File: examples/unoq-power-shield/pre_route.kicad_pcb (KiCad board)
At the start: 4 copper layers, 53.3 x 68.6 mm, 56 parts, among them J1 VIN 7-24V, J10 UNO PWR, J11 UNO ANALOG, J12 UNO D0-D7, J13 UNO D8-SCL, J2 5V OUT, J3 Qwiic, J4 Qwiic, J5 5V IO, Q1 BSS138LT1G, Q2 BSS138LT1G, Q3 BSS138LT1G, Q4 BSS138LT1G, Q5 AO4407A, U1 TPS54331DDAR, U2 INA226AIDGSR

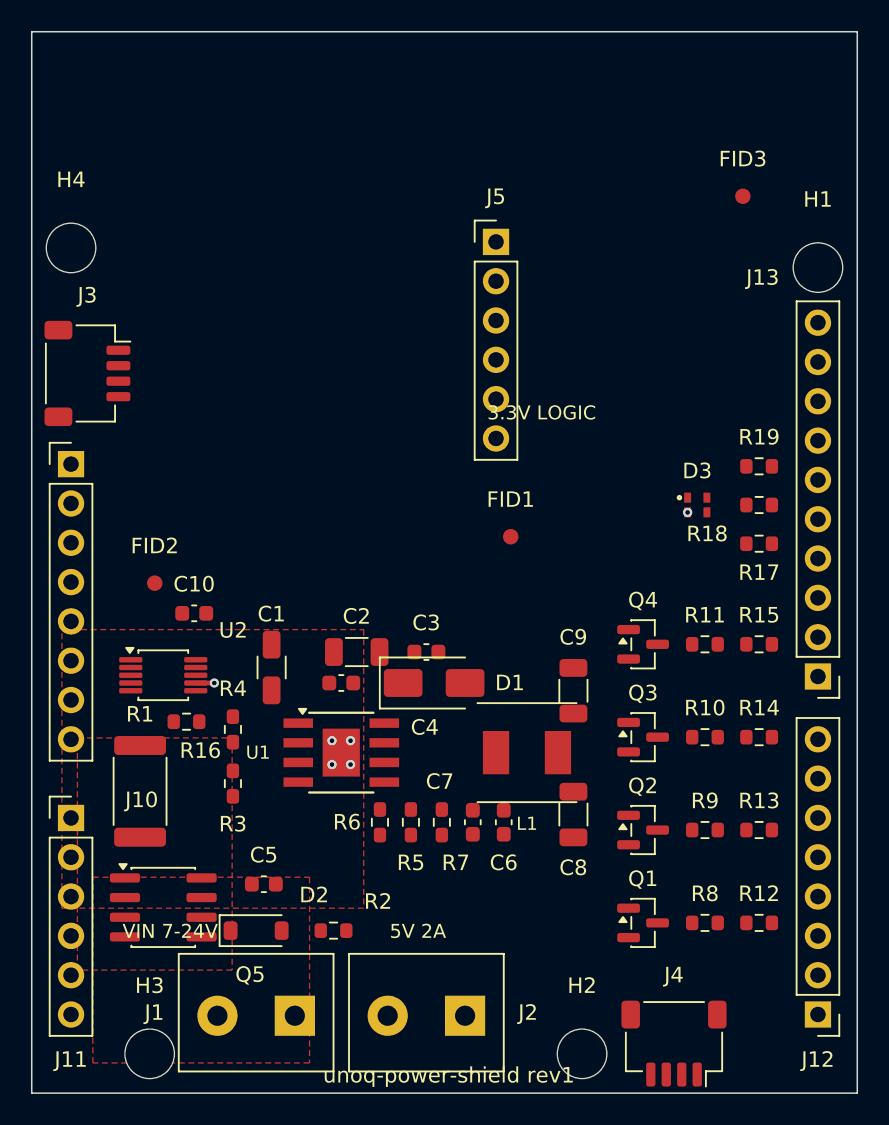
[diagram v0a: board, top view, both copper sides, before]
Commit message: Carry the silk fix into the pre-route snapshot too
route.py restarts from pre_route.kicad_pcb (`shutil.copyfile(snapshot,
board)` at step 0), so the snapshot still holding "3.3V LOGIC" on J5's
pads meant the next `make route` would have silently reinstated the
defect over the corrected board — with every gate still green, because
the gates would then be measuring the reverted silk.

Re-ran silk_finish against the snapshot with the corrected board.toml,
which is the same pass and order the build uses to produce it (zones ->
fanout -> fiducials -> keepouts -> silk -> fill -> snapshot). Warnings
empty; no copper touched.

Co-Authored-By: Claude Opus 5 (1M context) <noreply@anthropic.com>
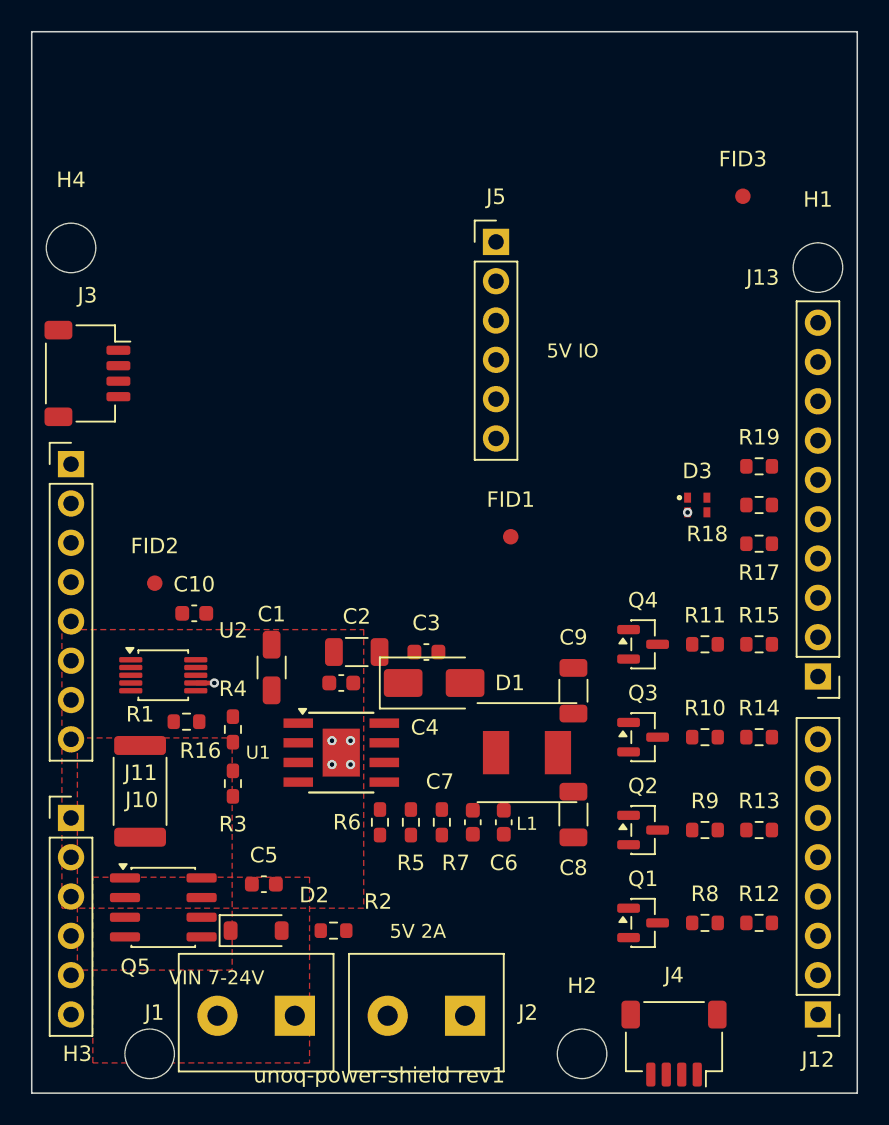
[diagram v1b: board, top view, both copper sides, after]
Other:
- board text added: "5V IO"
- board text removed: "3.3V LOGIC"

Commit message: Example: rotate J4 to face its edge, rebuild; all gates pass
J4 (Qwiic, SM04B-SRSS-TB) was at rotation 180 with its socket opening
into the board. Floorplan now rotation 0, y 3.2 -> 3.4 so the MP tabs
clear the 0.5 mm edge rule by 0.625 mm; the J4 copper_edge_clearance
ledger entry (a symptom of the rotation) is removed.

Rebuilt from netlist.csv in the pinned container (KiCad 10.0.5,
Freerouting 1.9.0) with the fixed pipeline. make check passes:
ERC 0 errors; pad angles all correct; DRC x5 13 errors, all ledgered,
identical every run, 0 unconnected, no stale entries; check_placement
11/0; validate_gerbers 15/0 with IPC-D-356 = netlist.csv 159/159.
drc_report.json, erc_report.json and img/*.png regenerated from the
rebuilt board. Still unfabricated; stock check and committing the exact
ordered package remain for order time (rev-1-plan.md).

Co-Authored-By: Claude Opus 5.5 <noreply@anthropic.com>
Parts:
- moved J4 0.20 mm to (163.3, 135.9), turned to 0 degrees
